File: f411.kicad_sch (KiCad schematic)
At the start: 16 parts, among them J18 THTPad, J21 Conn_2x02_Pin, SW1 SW_Push, SW2 SW_Push, U5 STM32F411CEUx

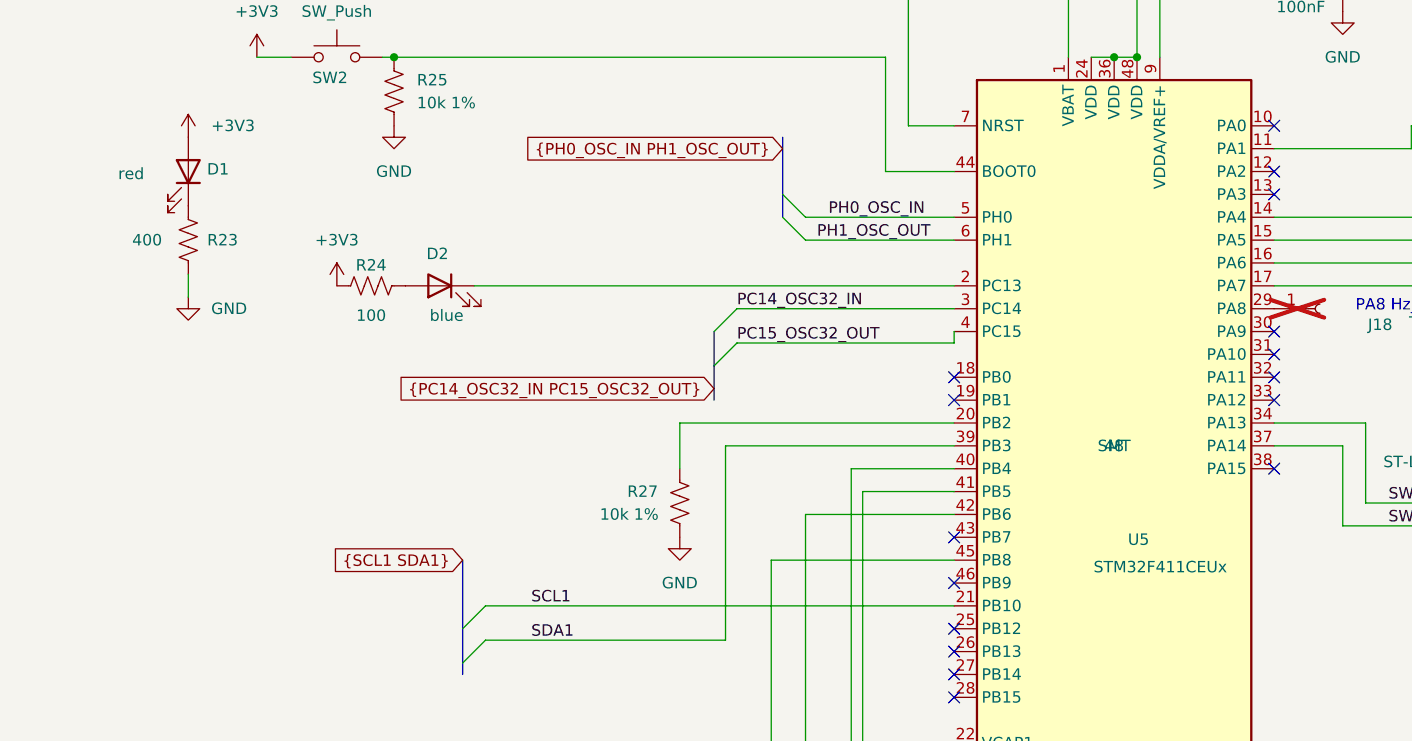
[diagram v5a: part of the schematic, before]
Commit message: As made,  t16-F411 v0.2.0 2025-05, with added notes about needed fixes and results from some testing.
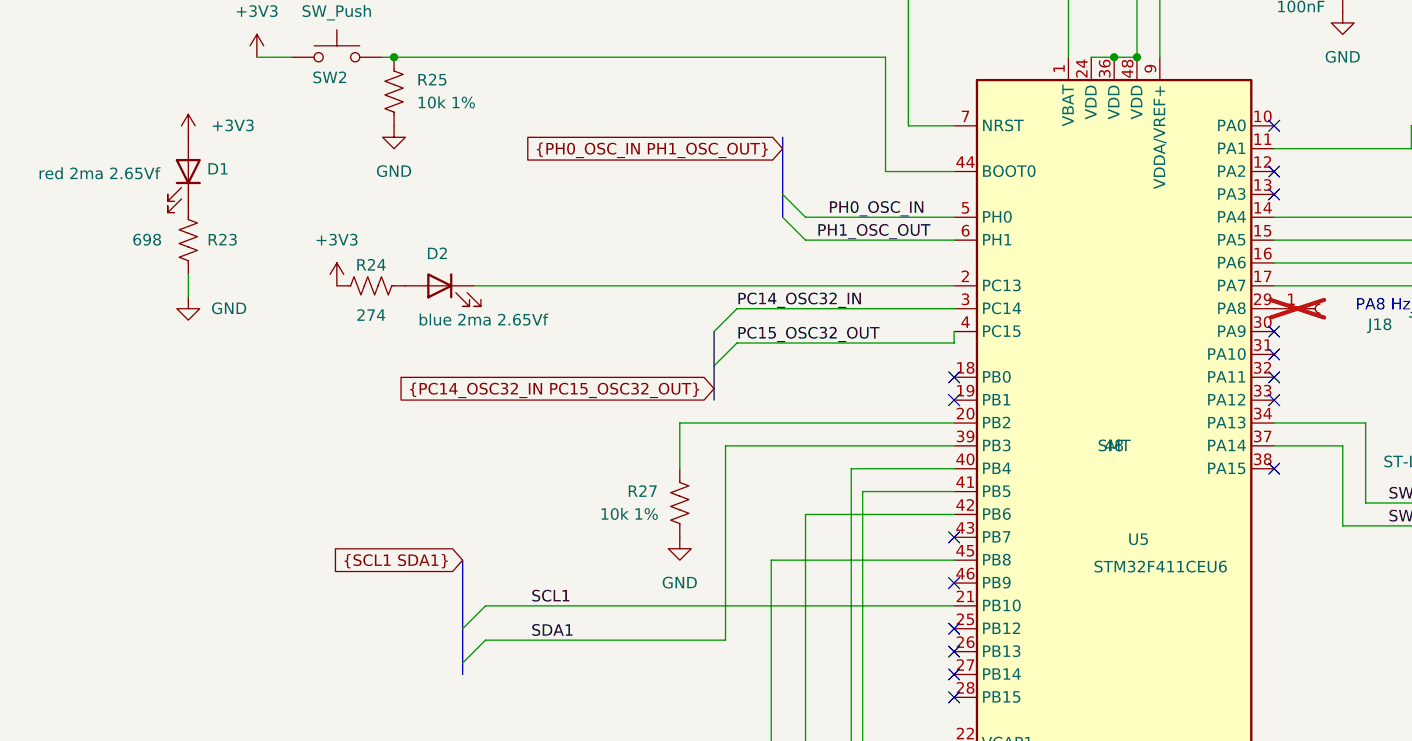
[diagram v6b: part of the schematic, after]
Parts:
- C14: Manufacturer (none) -> Samsung; MfgPart (none) -> CL10A475KP8NNNC
- C17, C9: Manufacturer (none) -> Samsung; MfgPart (none) -> CL10B104KB8NNNC
- D1: value red -> red 2ma 2.65Vf; Manufacturer Yongyu Photoelectric -> Kingbright; MfgPart yy0603re-nn1s0-t2ar4 -> APTD1608LSECK/J3-PF
- D2: value blue -> blue 2ma 2.65Vf; Manufacturer Yongyu Photoelectric -> Kingbright; MfgPart yy0603bl-nn1s0-t2ar4 -> APHD1608LVBC/D
- R23: value 400 -> 698; Manufacturer (none) -> Panasonic; MfgPart (none) -> ERJ3EKF6980V
- R24: value 100 -> 274; Manufacturer (none) -> Yageo; MfgPart (none) -> RC0603FR-07274RL
- R25, R26, R27: Manufacturer (none) -> Vishay; MfgPart (none) -> CRCW060310K0FKEA
- U5: value STM32F411CEUx -> STM32F411CEU6; MfgPart STM32F411CEUx -> STM32F411CEU6
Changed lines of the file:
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@@
 			)
 		)
-		(property "Datasheet" "~"
+		(property "Datasheet" ""
 			(at 64.77 63.5 0)
 			(effects
@@
 		)
 		(property "pads" "2"
+			(at 64.77 63.5 0)
+			(effects
+				(font
+					(size 1.27 1.27)
+				)
+				(hide yes)
+			)
+		)
+		(property "Manufacturer" "Vishay"
+			(at 64.77 63.5 0)
+			(effects
+				(font
+					(size 1.27 1.27)
+				)
+				(hide yes)
+			)
+		)
+		(property "MfgPart" "CRCW060310K0FKEA"
 			(at 64.77 63.5 0)
 			(effects
@@
 			)
 		)
-		(property "Datasheet" "~"
+		(property "Datasheet" ""
 			(at 123.19 139.7 0)
 			(effects
@@
 		)
 		(property "pads" "2"
+			(at 123.19 139.7 0)
+			(effects
+				(font
+					(size 1.27 1.27)
+				)
+				(hide yes)
+			)
+		)
+		(property "Manufacturer" "Samsung"
+			(at 123.19 139.7 0)
+			(effects
+				(font
+					(size 1.27 1.27)
+				)
+				(hide yes)
+			)
+		)
+		(property "MfgPart" "CL10A475KP8NNNC"
 			(at 123.19 139.7 0)
 			(effects
@@
 			)
 		)
-		(property "Value" "blue"
-			(at 70.612 88.392 0)
+		(property "Value" "blue 2ma 2.65Vf"
+			(at 74.676 88.9 0)
 			(effects
 				(font
@@
 			)
 		)
-		(property "Datasheet" "~"
+		(property "Datasheet" "https://www.kingbrightusa.com/images/catalog/SPEC/APHD1608LVBC-D.pdf"
 			(at 69.85 85.09 0)
 			(effects
@@
 			)
 		)
-		(property "Manufacturer" "Yongyu Photoelectric"
+		(property "Manufacturer" "Kingbright"
 			(at 69.85 85.09 0)
 			(effects
@@
 			)
 		)
-		(property "MfgPart" "yy0603bl-nn1s0-t2ar4"
+		(property "MfgPart" "APHD1608LVBC/D"
 			(at 69.85 85.09 0)
 			(effects
@@
 			)
 		)
-		(property "Datasheet" "~"
+		(property "Datasheet" ""
 			(at 96.52 109.22 0)
 			(effects
@@
 		)
 		(property "pads" "2"
+			(at 96.52 109.22 0)
+			(effects
+				(font
+					(size 1.27 1.27)
+				)
+				(hide yes)
+			)
+		)
+		(property "Manufacturer" "Vishay"
+			(at 96.52 109.22 0)
+			(effects
+				(font
+					(size 1.27 1.27)
+				)
+				(hide yes)
+			)
+		)
+		(property "MfgPart" "CRCW060310K0FKEA"
 			(at 96.52 109.22 0)
 			(effects
@@
 			)
 		)
-		(property "Datasheet" "~"
+		(property "Datasheet" ""
 			(at 67.31 44.45 0)
 			(effects
@@
 			)
 		)
+		(property "Manufacturer" "Samsung"
+			(at 67.31 44.45 90)
+			(effects
+				(font
+					(size 1.27 1.27)
+				)
+				(hide yes)
+			)
+		)
+		(property "MfgPart" "CL10B104KB8NNNC"
+			(at 67.31 44.45 90)
+			(effects
+				(font
+					(size 1.27 1.27)
+				)
+				(hide yes)
+			)
+		)
 		(pin "1"
 		)
@@
 			)
 		)
-		(property "Datasheet" "~"
+		(property "Datasheet" ""
 			(at 58.42 54.61 0)
 			(effects
@@
 			)
 		)
-		(property "Datasheet" "~"
+		(property "Datasheet" ""
 			(at 170.18 50.8 0)
 			(effects
@@
 			)
 		)
+		(property "Manufacturer" "Samsung"
+			(at 170.18 50.8 0)
+			(effects
+				(font
+					(size 1.27 1.27)
+				)
+				(hide yes)
+			)
+		)
+		(property "MfgPart" "CL10B104KB8NNNC"
+			(at 170.18 50.8 0)
+			(effects
+				(font
+					(size 1.27 1.27)
+				)
+				(hide yes)
+			)
+		)
 		(pin "1"
 		)
@@
 			)
 		)
-		(property "Datasheet" "~"
+		(property "Datasheet" ""
 			(at 71.12 34.29 0)
 			(effects
@@
 			)
 		)
-		(property "Value" "STM32F411CEUx"
+		(property "Value" "STM32F411CEU6"
 			(at 142.494 116.332 0)
 			(effects
@@
 			)
 		)
-		(property "MfgPart" "STM32F411CEUx"
+		(property "MfgPart" "STM32F411CEU6"
 			(at 144.78 102.87 0)
 			(effects
@@
 			)
 		)
-		(property "Datasheet" "~"
+		(property "Datasheet" ""
 			(at 170.18 43.18 0)
 			(effects
@@
 			)
 		)
-		(property "Value" "red"
-			(at 35.56 72.644 90)
+		(property "Value" "red 2ma 2.65Vf"
+			(at 32.004 72.644 90)
 			(effects
 				(font
@@
 			)
 		)
-		(property "Datasheet" "~"
+		(property "Datasheet" "https://www.digikey.cn/en/products/detail/kingbright/APTD1608LSECK-J3-PF/5177446"
 			(at 41.91 72.39 0)
 			(effects
@@
 			)
 		)
-		(property "Manufacturer" "Yongyu Photoelectric"
+		(property "Manufacturer" "Kingbright"
 			(at 41.91 72.39 0)
 			(effects
@@
 			)
 		)
-		(property "MfgPart" "yy0603re-nn1s0-t2ar4"
+		(property "MfgPart" "APTD1608LSECK/J3-PF"
 			(at 41.91 72.39 0)
 			(effects
@@
 			)
 		)
-		(property "Datasheet" "~"
+		(property "Datasheet" ""
 			(at 93.98 40.64 0)
 			(effects
@@
 		)
 		(property "pads" "2"
+			(at 93.98 40.64 0)
+			(effects
+				(font
+					(size 1.27 1.27)
+				)
+				(hide yes)
+			)
+		)
+		(property "Manufacturer" "Vishay"
+			(at 93.98 40.64 0)
+			(effects
+				(font
+					(size 1.27 1.27)
+				)
+				(hide yes)
+			)
+		)
+		(property "MfgPart" "CRCW060310K0FKEA"
 			(at 93.98 40.64 0)
 			(effects
@@
 			)
 		)
-		(property "Value" "100"
+		(property "Value" "274"
 			(at 62.23 88.392 90)
 			(effects
@@
 			)
 		)
-		(property "Datasheet" "~"
+		(property "Datasheet" ""
 			(at 62.23 85.09 0)
 			(effects
@@
 			)
 		)
+		(property "Manufacturer" "Yageo"
+			(at 62.23 85.09 90)
+			(effects
+				(font
+					(size 1.27 1.27)
+				)
+				(hide yes)
+			)
+		)
+		(property "MfgPart" "RC0603FR-07274RL"
+			(at 62.23 85.09 90)
+			(effects
+				(font
+					(size 1.27 1.27)
+				)
+				(hide yes)
+			)
+		)
 		(pin "1"
 		)
@@
 			)
 		)
-		(property "Value" "400"
+		(property "Value" "698"
 			(at 37.338 80.01 0)
 			(effects
@@
 			)
 		)
-		(property "Datasheet" "~"
+		(property "Datasheet" ""
 			(at 41.91 80.01 0)
 			(effects
@@
 			(at 41.91 80.01 0)
 			(effects
+				(font
+					(size 1.27 1.27)
+				)
+				(hide yes)
+			)
+		)
+		(property "Manufacturer" "Panasonic"
+			(at 41.91 80.01 0)
+			(effects
+				(font
+					(size 1.27 1.27)
+				)
+				(hide yes)
+			)
+		)
+		(property "MfgPart" "ERJ3EKF6980V"
+			(at 41.91 80.01 0)
+			(effects

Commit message: Most post v0.2.0 fixes done. About to mess with GND_ANT zone and net.
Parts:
- J18: value THTPad -> a8 MCO
- SW1: value SW_Push -> RST
- SW2: value SW_Push -> BT0
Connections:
- net SCL1: now also U5.45 (PB8); no longer U5.21 (PB10)
- net SCL2: now also U5.21 (PB10); no longer U5.45 (PB8)
- net SDA1: now also U5.46 (PB9); no longer U5.39 (PB3)
- net SDA2: now also U5.39 (PB3); no longer U5.42 (PB6)
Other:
- note removed: "PA8 Hz_out"
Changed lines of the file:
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@@
 		(rev "v0.1.1")
-	)
-	(text "PA8 Hz_out"
-		(exclude_from_sim no)
-		(at 176.53 87.376 0)
-		(effects
-			(font
-				(size 1.27 1.27)
-			)
-		)
 	)
 	(junction
@@
 	)
 	(no_connect
+		(at 127 110.49)
+	)
+	(no_connect
 		(at 127 128.27)
-	)
-	(no_connect
-		(at 127 118.11)
 	)
 	(no_connect
@@
 		)
 	)
-	(wire
-		(pts
-			(xy 127 110.49) (xy 110.49 110.49)
-		)
-		(stroke
-			(width 0)
-			(type default)
-		)
-	)
 	(bus
 		(pts
@@
 	(wire
 		(pts
+			(xy 110.49 144.78) (xy 110.49 118.11)
+		)
+		(stroke
+			(width 0)
+			(type default)
+		)
+	)
+	(wire
+		(pts
 			(xy 142.24 59.69) (xy 144.78 59.69)
 		)
@@
 	(wire
 		(pts
-			(xy 110.49 110.49) (xy 110.49 144.78)
-		)
-		(stroke
-			(width 0)
-			(type default)
-		)
-	)
-	(wire
-		(pts
 			(xy 102.87 91.44) (xy 127 91.44)
 		)
@@
 		(pts
 			(xy 64.77 59.69) (xy 119.38 59.69)
+		)
+		(stroke
+			(width 0)
+			(type default)
+		)
+	)
+	(wire
+		(pts
+			(xy 110.49 118.11) (xy 127 118.11)
 		)
 		(stroke
@@
 		)
 	)
-	(label "SDA2"
+	(label "SDA1"
 		(at 74.93 144.78 0)
 		(effects
@@
 		)
 	)
-	(label "SDA1"
+	(label "SDA2"
 		(at 80.01 124.46 0)
 		(effects
@@
 		)
 	)
-	(label "SCL1"
+	(label "SCL2"
 		(at 80.01 120.65 0)
 		(effects
@@
 		)
 	)
-	(label "SCL2"
+	(label "SCL1"
 		(at 74.93 140.97 0)
 		(effects
@@
 		)
 	)
-	(global_label "{SCL2 SDA2}"
+	(global_label "{SCL1 SDA1}"
 		(shape input)
 		(at 72.39 139.7 180)
@@
 		)
 	)
-	(global_label "{SCL1 SDA1}"
+	(global_label "{SCL2 SDA2}"
 		(shape input)
 		(at 72.39 115.57 180)
@@
 			)
 		)
-		(property "Value" "THTPad"
-			(at 177.546 89.154 0)
+		(property "Value" "a8 MCO"
+			(at 171.958 87.376 0)
 			(effects
 				(font
@@
 			)
 		)
-		(property "Value" "SW_Push"
+		(property "Value" "BT0"
 			(at 58.42 54.61 0)
 			(effects
@@
 			)
 		)
-		(property "Value" "SW_Push"
+		(property "Value" "RST"
 			(at 71.12 34.29 0)
 			(effects
